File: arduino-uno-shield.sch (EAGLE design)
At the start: 47 parts, among them T1 BC547, T2 BC547, T3 BC547, T4 BC547, T5 BC547, T6 BC547, T7 BC547, U1 SN74HC595N

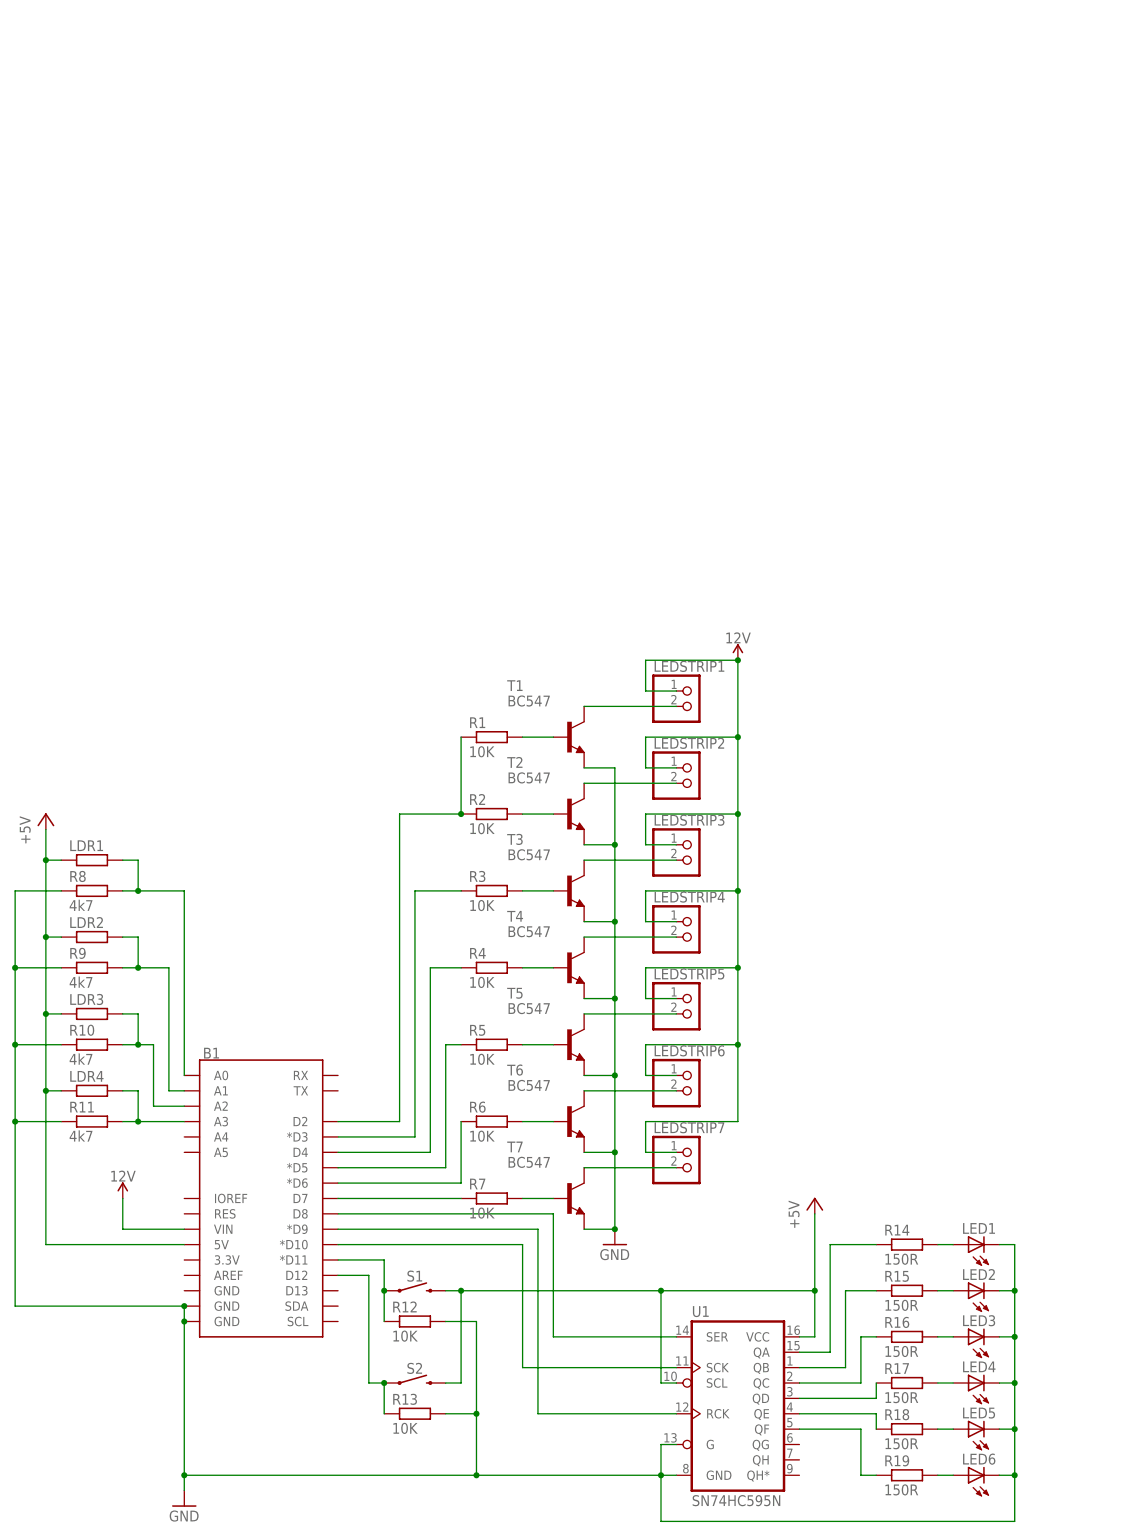
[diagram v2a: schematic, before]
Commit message: power jack added
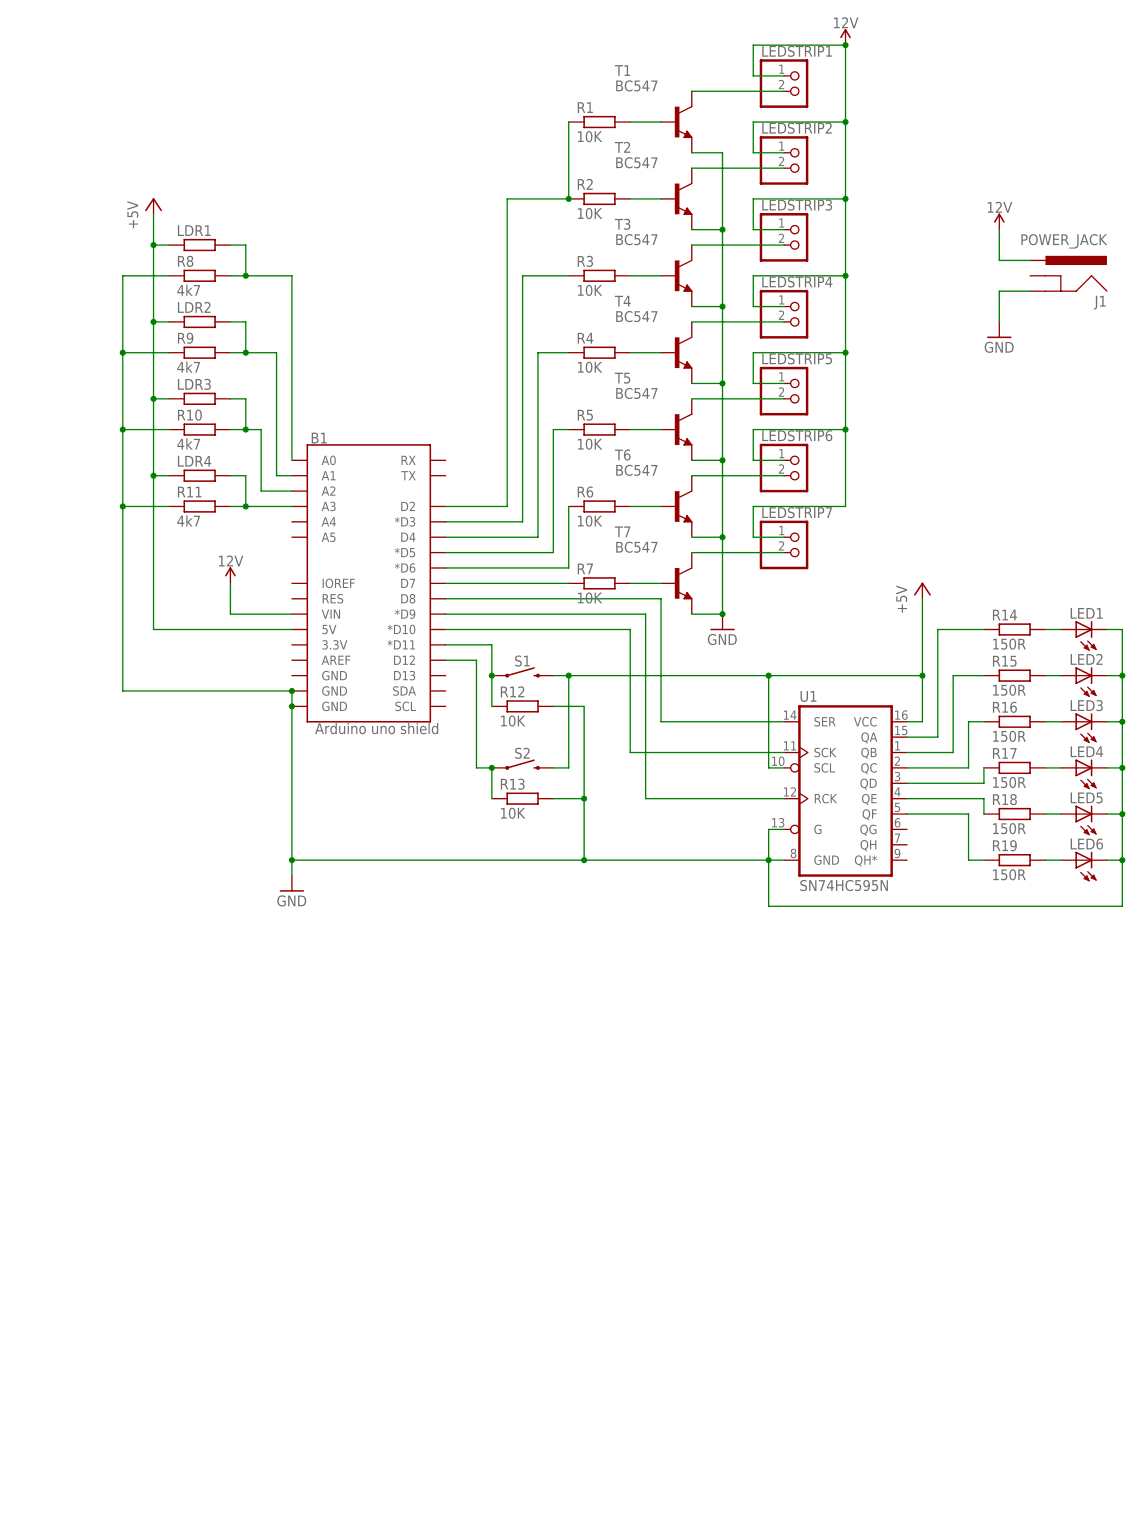
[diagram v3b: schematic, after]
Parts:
- added J1: POWER_JACK, SparkFun-Connectors:POWER_JACK
- B1: value ARDUINO_UNO_R3_SHIELDUNO_R3_SHIELD_NOLABELS_LOCK -> Arduino uno shield
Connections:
- net 12V: now also J1.PWR
- net GND: now also J1.GND
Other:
- moved on the sheet: B1, LDR1, LDR2, LDR3, LDR4, LED1, LED2, LED3, LED4, LED5, LED6, LEDSTRIP1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
